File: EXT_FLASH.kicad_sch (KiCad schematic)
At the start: 0 parts

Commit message: completed USB-C wiring and added flash
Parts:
- added U3: W25Q16JVUXIQ, symbol ESP32-S3_DB:W25Q64JV
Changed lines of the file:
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@@
 (kicad_sch (version 20230121) (generator eeschema)
   (paper "A4")
+  (symbol (lib_id "ESP32-S3_DB:W25Q64JV") (at 146.05 97.155 0) (unit 1)
+    (in_bom yes) (on_board yes) (dnp no)
+    (property "Reference" "U3" (at 143.51 83.185 0)
+      (effects (font (size 1.27 1.27)))
+    )
+    (property "Value" "W25Q16JVUXIQ" (at 143.51 85.09 0)
+      (effects (font (size 1.27 1.27)))
+    )
+    (property "Footprint" "" (at 146.05 97.155 0)
+      (effects (font (size 1.27 1.27)) hide)
+    )
+    (property "Datasheet" "" (at 146.05 97.155 0)
+      (effects (font (size 1.27 1.27)) hide)
+    )
+    (pin "1")
+    (pin "2")
+    (pin "3")
+    (pin "4")
+    (pin "5")
+    (pin "6")
+    (pin "7")
+    (pin "8")
+    (instances
+      (project "ESP32-S3_DB"
+        (path "/b7fc4bd3-c219-4455-832b-8d795385dcf1/4fcab1f4-10cc-47e3-9bc8-be24b657a388"
+          (reference "U3") (unit 1)
+        )
+      )
+    )
+  )
 )

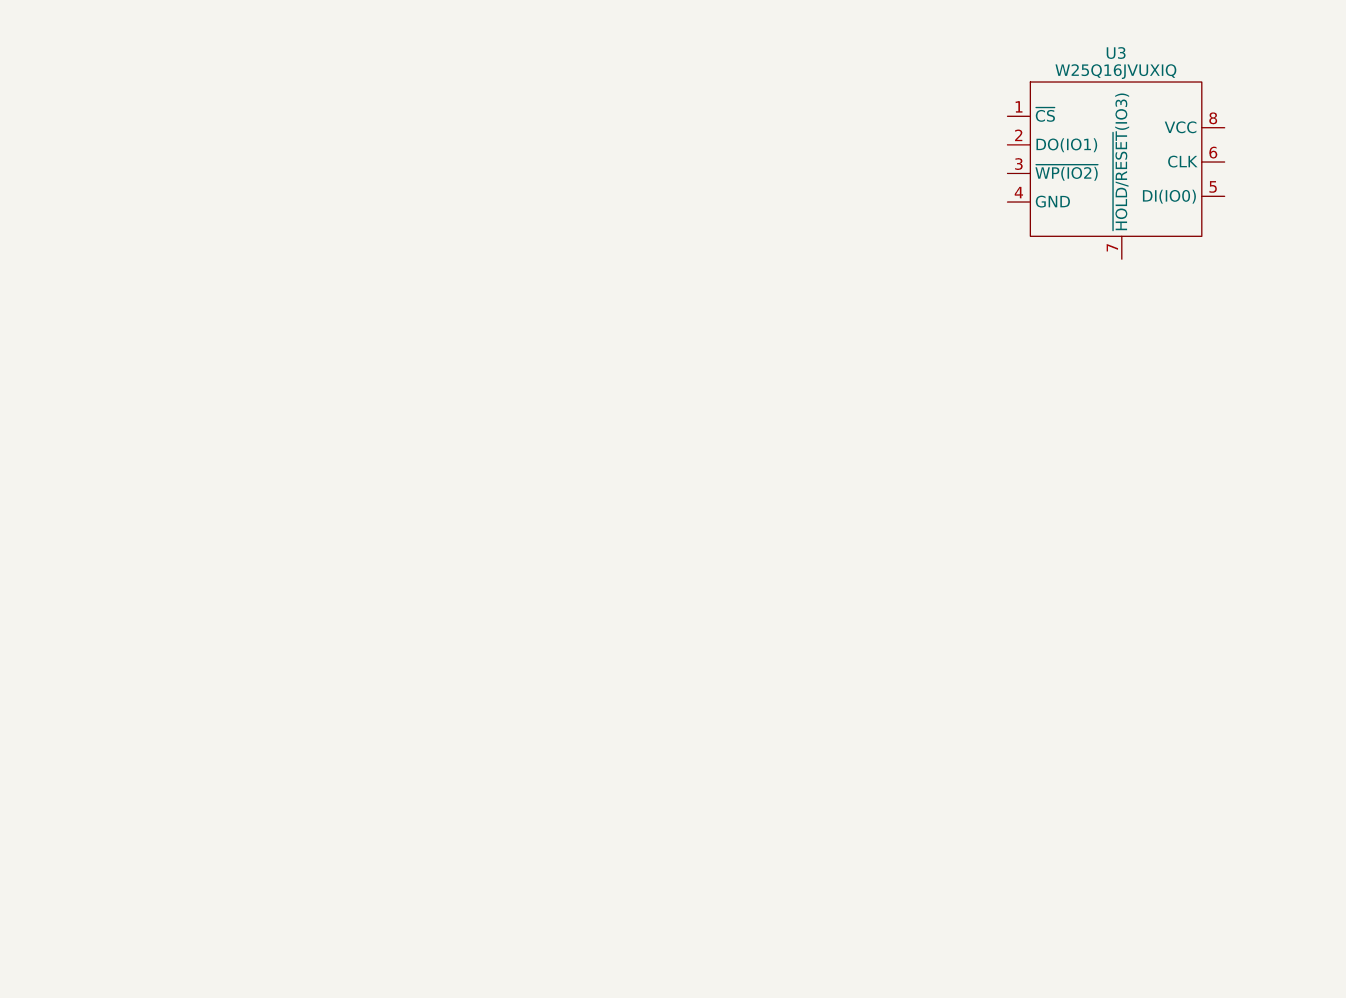
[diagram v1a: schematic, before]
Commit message: Added USB-To-UART Converter
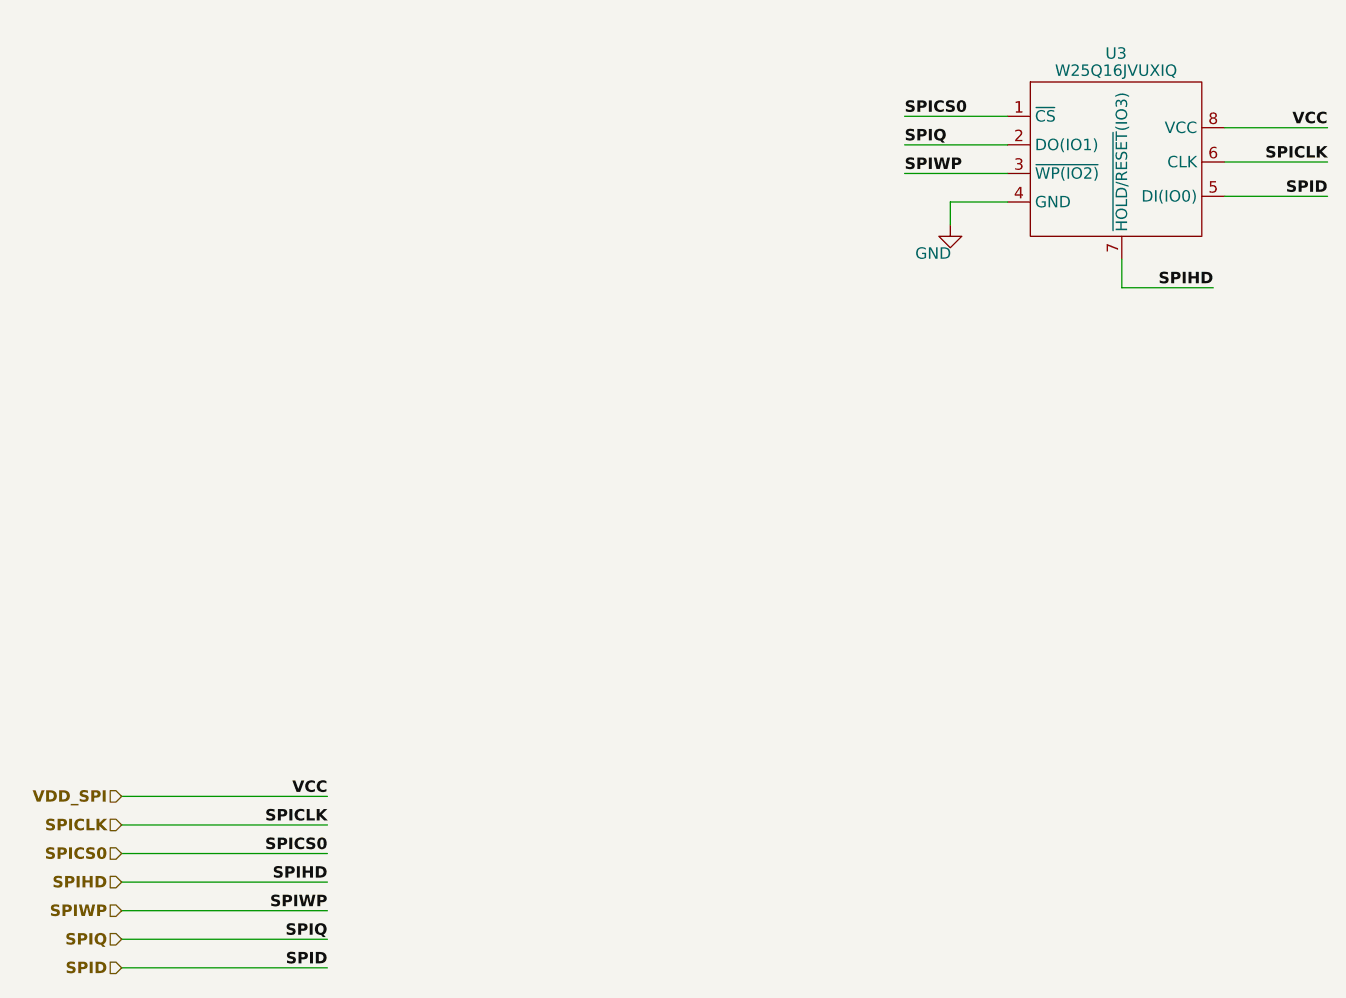
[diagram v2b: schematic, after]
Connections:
- net SPICS0: now reaches U3.1 (~{CS})
- net SPIQ: now reaches U3.2 (DO(IO1))
- net SPIWP: now reaches U3.3 (~{WP(IO2)})
- net GND: now reaches U3.4 (GND)
- net SPID: now reaches U3.5 (DI(IO0))
- net SPICLK: now reaches U3.6 (CLK)
- net SPIHD: now reaches U3.7 (~{HOLD/RESET}(IO3))
- net VDD_SPI: now reaches U3.8 (VCC)
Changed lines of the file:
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@@
 (kicad_sch (version 20230121) (generator eeschema)
   (paper "A4")
+  (wire (pts (xy 125.095 102.235) (xy 125.095 99.695))
+    (stroke (width 0) (type default))
+  )
+  (wire (pts (xy 154.305 109.22) (xy 144.145 109.22))
+    (stroke (width 0) (type default))
+  )
+  (wire (pts (xy 55.88 175.26) (xy 33.02 175.26))
+    (stroke (width 0) (type default))
+  )
+  (wire (pts (xy 55.88 184.785) (xy 33.02 184.785))
+    (stroke (width 0) (type default))
+  )
+  (wire (pts (xy 125.095 99.695) (xy 131.445 99.695))
+    (stroke (width 0) (type default))
+  )
+  (wire (pts (xy 120.015 96.52) (xy 131.445 96.52))
+    (stroke (width 0) (type default))
+  )
+  (wire (pts (xy 55.88 172.085) (xy 33.02 172.085))
+    (stroke (width 0) (type default))
+  )
+  (wire (pts (xy 120.015 93.345) (xy 131.445 93.345))
+    (stroke (width 0) (type default))
+  )
+  (wire (pts (xy 167.005 91.44) (xy 155.575 91.44))
+    (stroke (width 0) (type default))
+  )
+  (wire (pts (xy 55.88 168.91) (xy 33.02 168.91))
+    (stroke (width 0) (type default))
+  )
+  (wire (pts (xy 55.88 178.435) (xy 33.02 178.435))
+    (stroke (width 0) (type default))
+  )
+  (wire (pts (xy 144.145 109.22) (xy 144.145 106.045))
+    (stroke (width 0) (type default))
+  )
+  (wire (pts (xy 120.015 90.17) (xy 131.445 90.17))
+    (stroke (width 0) (type default))
+  )
+  (wire (pts (xy 167.005 95.25) (xy 155.575 95.25))
+    (stroke (width 0) (type default))
+  )
+  (wire (pts (xy 167.005 99.06) (xy 155.575 99.06))
+    (stroke (width 0) (type default))
+  )
+  (wire (pts (xy 55.88 165.735) (xy 33.02 165.735))
+    (stroke (width 0) (type default))
+  )
+  (wire (pts (xy 55.88 181.61) (xy 33.02 181.61))
+    (stroke (width 0) (type default))
+  )
+  (label "SPICLK" (at 167.005 95.25 180) (fields_autoplaced)
+    (effects (font (size 1.27 1.27) bold (color 0 0 255 1)) (justify right bottom))
+  )
+  (label "SPIHD" (at 154.305 109.22 180) (fields_autoplaced)
+    (effects (font (size 1.27 1.27) bold (color 0 0 255 1)) (justify right bottom))
+  )
+  (label "SPID" (at 55.88 184.785 180) (fields_autoplaced)
+    (effects (font (size 1.27 1.27) bold (color 0 0 255 1)) (justify right bottom))
+  )
+  (label "VCC" (at 167.005 91.44 180) (fields_autoplaced)
+    (effects (font (size 1.27 1.27) (thickness 0.254) bold (color 255 0 0 1)) (justify right bottom))
+  )
+  (label "SPIWP" (at 55.88 178.435 180) (fields_autoplaced)
+    (effects (font (size 1.27 1.27) bold (color 0 0 255 1)) (justify right bottom))
+  )
+  (label "SPICLK" (at 55.88 168.91 180) (fields_autoplaced)
+    (effects (font (size 1.27 1.27) bold (color 0 0 255 1)) (justify right bottom))
+  )
+  (label "SPICS0" (at 55.88 172.085 180) (fields_autoplaced)
+    (effects (font (size 1.27 1.27) bold (color 0 0 255 1)) (justify right bottom))
+  )
+  (label "SPICS0" (at 120.015 90.17 0) (fields_autoplaced)
+    (effects (font (size 1.27 1.27) bold (color 0 0 255 1)) (justify left bottom))
+  )
+  (label "SPIQ" (at 120.015 93.345 0) (fields_autoplaced)
+    (effects (font (size 1.27 1.27) bold (color 0 0 255 1)) (justify left bottom))
+  )
+  (label "SPIQ" (at 55.88 181.61 180) (fields_autoplaced)
+    (effects (font (size 1.27 1.27) bold (color 0 0 255 1)) (justify right bottom))
+  )
+  (label "SPIHD" (at 55.88 175.26 180) (fields_autoplaced)
+    (effects (font (size 1.27 1.27) bold (color 0 0 255 1)) (justify right bottom))
+  )
+  (label "SPID" (at 167.005 99.06 180) (fields_autoplaced)
+    (effects (font (size 1.27 1.27) bold (color 0 0 255 1)) (justify right bottom))
+  )
+  (label "SPIWP" (at 120.015 96.52 0) (fields_autoplaced)
+    (effects (font (size 1.27 1.27) bold (color 0 0 255 1)) (justify left bottom))
+  )
+  (label "VCC" (at 55.88 165.735 180) (fields_autoplaced)
+    (effects (font (size 1.27 1.27) (thickness 0.254) bold (color 255 0 0 1)) (justify right bottom))
+  )
+  (hierarchical_label "SPIWP" (shape input) (at 33.02 178.435 180) (fields_autoplaced)
+    (effects (font (size 1.27 1.27) (thickness 0.254) bold (color 0 0 255 1)) (justify right))
+  )
+  (hierarchical_label "SPICLK" (shape input) (at 33.02 168.91 180) (fields_autoplaced)
+    (effects (font (size 1.27 1.27) (thickness 0.254) bold (color 0 0 255 1)) (justify right))
+  )
+  (hierarchical_label "SPID" (shape input) (at 33.02 184.785 180) (fields_autoplaced)
+    (effects (font (size 1.27 1.27) (thickness 0.254) bold (color 0 0 255 1)) (justify right))
+  )
+  (hierarchical_label "SPIQ" (shape input) (at 33.02 181.61 180) (fields_autoplaced)
+    (effects (font (size 1.27 1.27) (thickness 0.254) bold (color 0 0 255 1)) (justify right))
+  )
+  (hierarchical_label "VDD_SPI" (shape input) (at 33.02 165.735 180) (fields_autoplaced)
+    (effects (font (size 1.27 1.27) (thickness 0.254) bold (color 255 0 0 1)) (justify right))
+  )
+  (hierarchical_label "SPICS0" (shape input) (at 33.02 172.085 180) (fields_autoplaced)
+    (effects (font (size 1.27 1.27) (thickness 0.254) bold (color 0 0 255 1)) (justify right))
+  )
+  (hierarchical_label "SPIHD" (shape input) (at 33.02 175.26 180) (fields_autoplaced)
+    (effects (font (size 1.27 1.27) (thickness 0.254) bold (color 0 0 255 1)) (justify right))
+  )
+  (symbol (lib_id "ESP32-S3_DB:GND") (at 125.095 102.235 0) (unit 1)
+    (in_bom yes) (on_board yes) (dnp no)
+    (property "Reference" "#PWR026" (at 125.095 108.585 0)
+      (effects (font (size 1.27 1.27)) hide)
+    )
+    (property "Value" "GND" (at 123.19 105.41 0)
+      (effects (font (size 1.27 1.27)))
+    )
+    (property "Footprint" "" (at 125.095 102.235 0)
+      (effects (font (size 1.27 1.27)) hide)
+    )
+    (property "Datasheet" "" (at 125.095 102.235 0)
+      (effects (font (size 1.27 1.27)) hide)
+    )
+    (pin "1")
+    (instances
+      (project "ESP32-S3_DB"
+        (path "/b7fc4bd3-c219-4455-832b-8d795385dcf1/4fcab1f4-10cc-47e3-9bc8-be24b657a388"
+          (reference "#PWR026") (unit 1)
+        )
+      )
+    )
+  )
   (symbol (lib_id "ESP32-S3_DB:W25Q64JV") (at 146.05 97.155 0) (unit 1)
     (in_bom yes) (on_board yes) (dnp no)
